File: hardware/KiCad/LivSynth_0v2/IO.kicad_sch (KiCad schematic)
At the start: 95 parts, among them J1 PJ398SM, J13 Jumper, J14 Jumper, J2 PJ398SM, J20 IDC, J3 PJ398SM, J4 IDC, Q6 2N3904, Q7 2N3904, SW6 SW_Push, U10 PCA9685PW, U11 PCA9685PW, U13 74HC165, U14 74HC165, U3 LM386

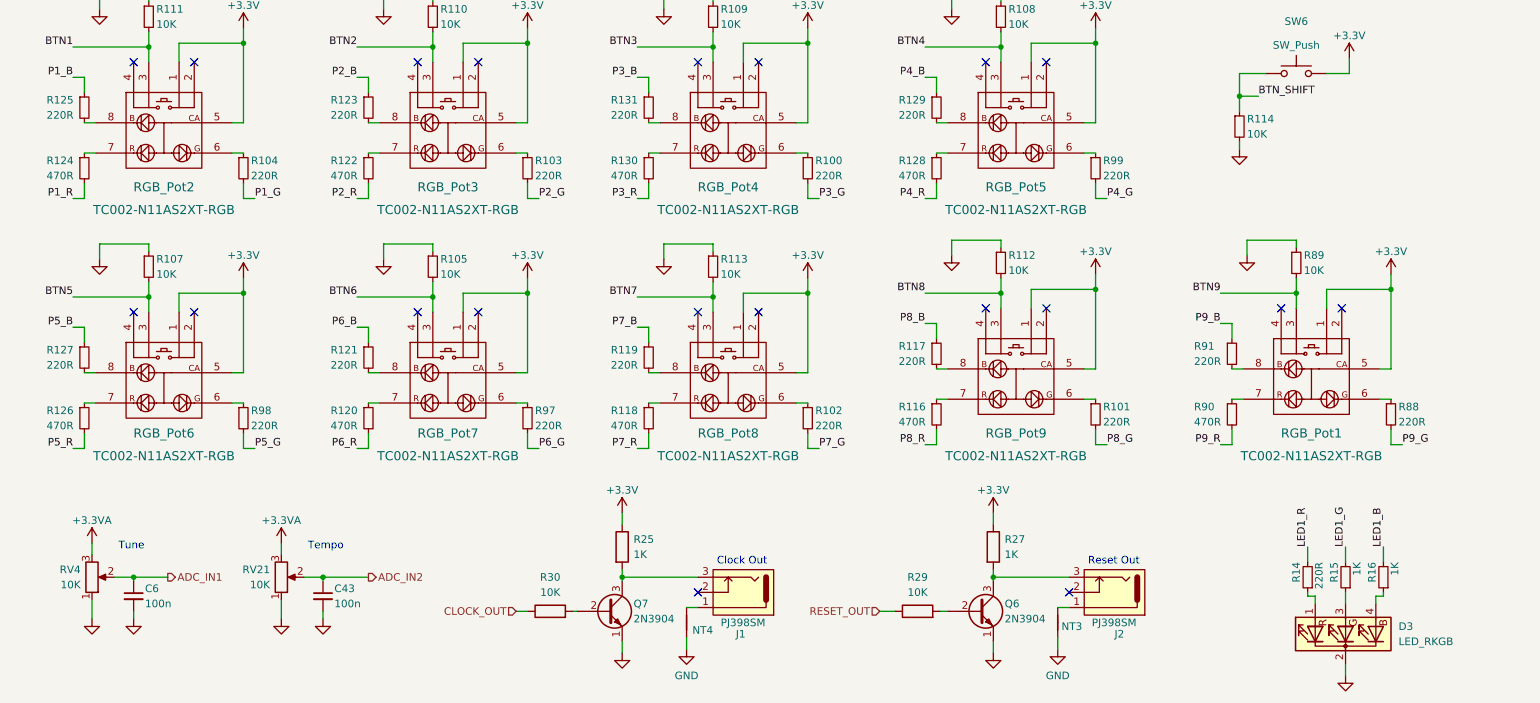
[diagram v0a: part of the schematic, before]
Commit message: Modify toggle switches (footprint and 3D model) Align R value designators Add JLC component placement checkup file
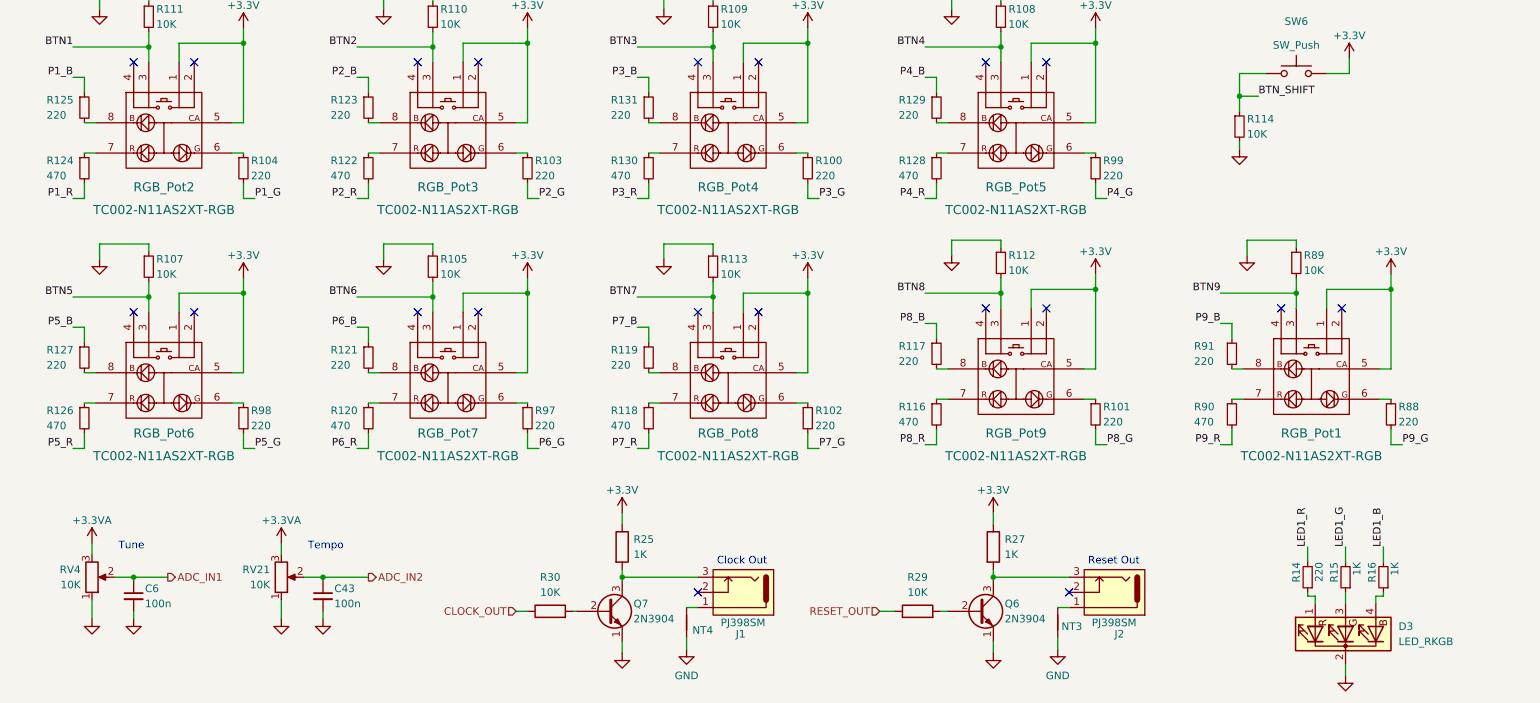
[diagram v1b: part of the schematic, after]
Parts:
- R100, R101, R102, R103, R104, R117, R119, R121, R123, R125, R127, R129, R131, R14, R88, R91, R97, R98, R99: value 220R -> 220
- R116, R118, R120, R122, R124, R126, R128, R130, R90: value 470R -> 470
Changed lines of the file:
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@@
       (effects (font (size 1.27 1.27)) (justify left))
     )
-    (property "Value" "220R" (id 1) (at 194.31 158.115 0)
+    (property "Value" "220" (id 1) (at 194.31 158.115 0)
       (effects (font (size 1.27 1.27)) (justify left))
     )
@@
       (effects (font (size 1.27 1.27)) (justify left))
     )
-    (property "Value" "220R" (id 1) (at 209.55 147.955 0)
+    (property "Value" "220" (id 1) (at 209.55 147.955 0)
       (effects (font (size 1.27 1.27)) (justify left))
     )
@@
       (effects (font (size 1.27 1.27)) (justify left))
     )
-    (property "Value" "220R" (id 1) (at 111.76 106.68 0)
+    (property "Value" "220" (id 1) (at 111.76 106.68 0)
       (effects (font (size 1.27 1.27)) (justify left))
     )
@@
       (effects (font (size 1.27 1.27)) (justify left))
     )
-    (property "Value" "220R" (id 1) (at 230.505 181.61 90)
+    (property "Value" "220" (id 1) (at 230.505 181.61 90)
       (effects (font (size 1.27 1.27)) (justify left))
     )
@@
       (effects (font (size 1.27 1.27)) (justify left))
     )
-    (property "Value" "220R" (id 1) (at 51.435 116.84 0)
+    (property "Value" "220" (id 1) (at 51.435 116.84 0)
       (effects (font (size 1.27 1.27)) (justify left))
     )
@@
       (effects (font (size 1.27 1.27)) (justify left))
     )
-    (property "Value" "470R" (id 1) (at 111.76 158.75 0)
+    (property "Value" "470" (id 1) (at 111.76 158.75 0)
       (effects (font (size 1.27 1.27)) (justify left))
     )
@@
       (effects (font (size 1.27 1.27)) (justify left))
     )
-    (property "Value" "220R" (id 1) (at 160.02 147.955 0)
+    (property "Value" "220" (id 1) (at 160.02 147.955 0)
       (effects (font (size 1.27 1.27)) (justify left))
     )
@@
       (effects (font (size 1.27 1.27)) (justify left))
     )
-    (property "Value" "220R" (id 1) (at 146.05 158.75 0)
+    (property "Value" "220" (id 1) (at 146.05 158.75 0)
       (effects (font (size 1.27 1.27)) (justify left))
     )
@@
       (effects (font (size 1.27 1.27)) (justify left))
     )
-    (property "Value" "220R" (id 1) (at 111.76 148.59 0)
+    (property "Value" "220" (id 1) (at 111.76 148.59 0)
       (effects (font (size 1.27 1.27)) (justify left))
     )
@@
       (effects (font (size 1.27 1.27)) (justify left))
     )
-    (property "Value" "220R" (id 1) (at 99.06 158.75 0)
+    (property "Value" "220" (id 1) (at 99.06 158.75 0)
       (effects (font (size 1.27 1.27)) (justify left))
     )
@@
       (effects (font (size 1.27 1.27)) (justify left))
     )
-    (property "Value" "470R" (id 1) (at 209.55 158.115 0)
+    (property "Value" "470" (id 1) (at 209.55 158.115 0)
       (effects (font (size 1.27 1.27)) (justify left))
     )
@@
       (effects (font (size 1.27 1.27)) (justify left))
     )
-    (property "Value" "220R" (id 1) (at 64.77 148.59 0)
+    (property "Value" "220" (id 1) (at 64.77 148.59 0)
       (effects (font (size 1.27 1.27)) (justify left))
     )
@@
       (effects (font (size 1.27 1.27)) (justify left))
     )
-    (property "Value" "220R" (id 1) (at 194.31 116.84 0)
+    (property "Value" "220" (id 1) (at 194.31 116.84 0)
       (effects (font (size 1.27 1.27)) (justify left))
     )
@@
       (effects (font (size 1.27 1.27)) (justify left))
     )
-    (property "Value" "220R" (id 1) (at 17.145 106.68 0)
+    (property "Value" "220" (id 1) (at 17.145 106.68 0)
       (effects (font (size 1.27 1.27)) (justify left))
     )
@@
       (effects (font (size 1.27 1.27)) (justify left))
     )
-    (property "Value" "220R" (id 1) (at 51.435 158.75 0)
+    (property "Value" "220" (id 1) (at 51.435 158.75 0)
       (effects (font (size 1.27 1.27)) (justify left))
     )
@@
       (effects (font (size 1.27 1.27)) (justify left))
     )
-    (property "Value" "470R" (id 1) (at 111.76 116.84 0)
+    (property "Value" "470" (id 1) (at 111.76 116.84 0)
       (effects (font (size 1.27 1.27)) (justify left))
     )
@@
       (effects (font (size 1.27 1.27)) (justify left))
     )
-    (property "Value" "470R" (id 1) (at 17.145 116.84 0)
+    (property "Value" "470" (id 1) (at 17.145 116.84 0)
       (effects (font (size 1.27 1.27)) (justify left))
     )
@@
       (effects (font (size 1.27 1.27)) (justify left))
     )
-    (property "Value" "220R" (id 1) (at 243.84 158.115 0)
+    (property "Value" "220" (id 1) (at 243.84 158.115 0)
       (effects (font (size 1.27 1.27)) (justify left))
     )
@@
       (effects (font (size 1.27 1.27)) (justify left))
     )
-    (property "Value" "220R" (id 1) (at 99.06 116.84 0)
+    (property "Value" "220" (id 1) (at 99.06 116.84 0)
       (effects (font (size 1.27 1.27)) (justify left))
     )
@@
       (effects (font (size 1.27 1.27)) (justify left))
     )
-    (property "Value" "470R" (id 1) (at 64.77 116.84 0)
+    (property "Value" "470" (id 1) (at 64.77 116.84 0)
       (effects (font (size 1.27 1.27)) (justify left))
     )
@@
       (effects (font (size 1.27 1.27)) (justify left))
     )
-    (property "Value" "470R" (id 1) (at 64.77 158.75 0)
+    (property "Value" "470" (id 1) (at 64.77 158.75 0)
       (effects (font (size 1.27 1.27)) (justify left))
     )
@@
       (effects (font (size 1.27 1.27)) (justify left))
     )
-    (property "Value" "220R" (id 1) (at 160.02 106.68 0)
+    (property "Value" "220" (id 1) (at 160.02 106.68 0)
       (effects (font (size 1.27 1.27)) (justify left))
     )
@@
       (effects (font (size 1.27 1.27)) (justify left))
     )
-    (property "Value" "220R" (id 1) (at 146.05 116.84 0)
+    (property "Value" "220" (id 1) (at 146.05 116.84 0)
       (effects (font (size 1.27 1.27)) (justify left))
     )
@@
       (effects (font (size 1.27 1.27)) (justify left))
     )
-    (property "Value" "470R" (id 1) (at 160.02 116.84 0)
+    (property "Value" "470" (id 1) (at 160.02 116.84 0)
       (effects (font (size 1.27 1.27)) (justify left))
     )
@@
       (effects (font (size 1.27 1.27)) (justify left))
     )
-    (property "Value" "220R" (id 1) (at 64.77 106.68 0)
+    (property "Value" "220" (id 1) (at 64.77 106.68 0)
       (effects (font (size 1.27 1.27)) (justify left))
     )
@@
       (effects (font (size 1.27 1.27)) (justify left))
     )
-    (property "Value" "470R" (id 1) (at 160.02 158.115 0)
+    (property "Value" "470" (id 1) (at 160.02 158.115 0)
       (effects (font (size 1.27 1.27)) (justify left))
     )
@@
       (effects (font (size 1.27 1.27)) (justify left))
     )
-    (property "Value" "220R" (id 1) (at 17.145 148.59 0)
+    (property "Value" "220" (id 1) (at 17.145 148.59 0)
       (effects (font (size 1.27 1.27)) (justify left))
     )
@@
       (effects (font (size 1.27 1.27)) (justify left))
     )
-    (property "Value" "470R" (id 1) (at 17.145 158.75 0)
-      (effects (font (size 1.27 1.27)) (justify left))
-    )
+    (property "Value" "470" (id 1) (at 17.145 158.75 0)
+      (effects (font (size 1.27 1.27)) (justify left))
+    )

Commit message: Create new 0v3 folder
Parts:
- R100, R101, R102, R103, R104, R117, R119, R121, R123, R125, R127, R129, R131, R14, R88, R91, R97, R98, R99: value 220 -> 220R
- R116, R118, R120, R122, R124, R126, R128, R130, R90: value 470 -> 470R
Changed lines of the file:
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@@
       (effects (font (size 1.27 1.27)) (justify left))
     )
-    (property "Value" "220" (id 1) (at 194.31 158.115 0)
+    (property "Value" "220R" (id 1) (at 194.31 158.115 0)
       (effects (font (size 1.27 1.27)) (justify left))
     )
@@
       (effects (font (size 1.27 1.27)) (justify left))
     )
-    (property "Value" "220" (id 1) (at 209.55 147.955 0)
+    (property "Value" "220R" (id 1) (at 209.55 147.955 0)
       (effects (font (size 1.27 1.27)) (justify left))
     )
@@
       (effects (font (size 1.27 1.27)) (justify left))
     )
-    (property "Value" "220" (id 1) (at 111.76 106.68 0)
+    (property "Value" "220R" (id 1) (at 111.76 106.68 0)
       (effects (font (size 1.27 1.27)) (justify left))
     )
@@
       (effects (font (size 1.27 1.27)) (justify left))
     )
-    (property "Value" "220" (id 1) (at 230.505 181.61 90)
+    (property "Value" "220R" (id 1) (at 230.505 181.61 90)
       (effects (font (size 1.27 1.27)) (justify left))
     )
@@
       (effects (font (size 1.27 1.27)) (justify left))
     )
-    (property "Value" "220" (id 1) (at 51.435 116.84 0)
+    (property "Value" "220R" (id 1) (at 51.435 116.84 0)
       (effects (font (size 1.27 1.27)) (justify left))
     )
@@
       (effects (font (size 1.27 1.27)) (justify left))
     )
-    (property "Value" "470" (id 1) (at 111.76 158.75 0)
+    (property "Value" "470R" (id 1) (at 111.76 158.75 0)
       (effects (font (size 1.27 1.27)) (justify left))
     )
@@
       (effects (font (size 1.27 1.27)) (justify left))
     )
-    (property "Value" "220" (id 1) (at 160.02 147.955 0)
+    (property "Value" "220R" (id 1) (at 160.02 147.955 0)
       (effects (font (size 1.27 1.27)) (justify left))
     )
@@
       (effects (font (size 1.27 1.27)) (justify left))
     )
-    (property "Value" "220" (id 1) (at 146.05 158.75 0)
+    (property "Value" "220R" (id 1) (at 146.05 158.75 0)
       (effects (font (size 1.27 1.27)) (justify left))
     )
@@
       (effects (font (size 1.27 1.27)) (justify left))
     )
-    (property "Value" "220" (id 1) (at 111.76 148.59 0)
+    (property "Value" "220R" (id 1) (at 111.76 148.59 0)
       (effects (font (size 1.27 1.27)) (justify left))
     )
@@
       (effects (font (size 1.27 1.27)) (justify left))
     )
-    (property "Value" "220" (id 1) (at 99.06 158.75 0)
+    (property "Value" "220R" (id 1) (at 99.06 158.75 0)
       (effects (font (size 1.27 1.27)) (justify left))
     )
@@
       (effects (font (size 1.27 1.27)) (justify left))
     )
-    (property "Value" "470" (id 1) (at 209.55 158.115 0)
+    (property "Value" "470R" (id 1) (at 209.55 158.115 0)
       (effects (font (size 1.27 1.27)) (justify left))
     )
@@
       (effects (font (size 1.27 1.27)) (justify left))
     )
-    (property "Value" "220" (id 1) (at 64.77 148.59 0)
+    (property "Value" "220R" (id 1) (at 64.77 148.59 0)
       (effects (font (size 1.27 1.27)) (justify left))
     )
@@
       (effects (font (size 1.27 1.27)) (justify left))
     )
-    (property "Value" "220" (id 1) (at 194.31 116.84 0)
+    (property "Value" "220R" (id 1) (at 194.31 116.84 0)
       (effects (font (size 1.27 1.27)) (justify left))
     )
@@
       (effects (font (size 1.27 1.27)) (justify left))
     )
-    (property "Value" "220" (id 1) (at 17.145 106.68 0)
+    (property "Value" "220R" (id 1) (at 17.145 106.68 0)
       (effects (font (size 1.27 1.27)) (justify left))
     )
@@
       (effects (font (size 1.27 1.27)) (justify left))
     )
-    (property "Value" "220" (id 1) (at 51.435 158.75 0)
+    (property "Value" "220R" (id 1) (at 51.435 158.75 0)
       (effects (font (size 1.27 1.27)) (justify left))
     )
@@
       (effects (font (size 1.27 1.27)) (justify left))
     )
-    (property "Value" "470" (id 1) (at 111.76 116.84 0)
+    (property "Value" "470R" (id 1) (at 111.76 116.84 0)
       (effects (font (size 1.27 1.27)) (justify left))
     )
@@
       (effects (font (size 1.27 1.27)) (justify left))
     )
-    (property "Value" "470" (id 1) (at 17.145 116.84 0)
+    (property "Value" "470R" (id 1) (at 17.145 116.84 0)
       (effects (font (size 1.27 1.27)) (justify left))
     )
@@
       (effects (font (size 1.27 1.27)) (justify left))
     )
-    (property "Value" "220" (id 1) (at 243.84 158.115 0)
+    (property "Value" "220R" (id 1) (at 243.84 158.115 0)
       (effects (font (size 1.27 1.27)) (justify left))
     )
@@
       (effects (font (size 1.27 1.27)) (justify left))
     )
-    (property "Value" "220" (id 1) (at 99.06 116.84 0)
+    (property "Value" "220R" (id 1) (at 99.06 116.84 0)
       (effects (font (size 1.27 1.27)) (justify left))
     )
@@
       (effects (font (size 1.27 1.27)) (justify left))
     )
-    (property "Value" "470" (id 1) (at 64.77 116.84 0)
+    (property "Value" "470R" (id 1) (at 64.77 116.84 0)
       (effects (font (size 1.27 1.27)) (justify left))
     )
@@
       (effects (font (size 1.27 1.27)) (justify left))
     )
-    (property "Value" "470" (id 1) (at 64.77 158.75 0)
+    (property "Value" "470R" (id 1) (at 64.77 158.75 0)
       (effects (font (size 1.27 1.27)) (justify left))
     )
@@
       (effects (font (size 1.27 1.27)) (justify left))
     )
-    (property "Value" "220" (id 1) (at 160.02 106.68 0)
+    (property "Value" "220R" (id 1) (at 160.02 106.68 0)
       (effects (font (size 1.27 1.27)) (justify left))
     )
@@
       (effects (font (size 1.27 1.27)) (justify left))
     )
-    (property "Value" "220" (id 1) (at 146.05 116.84 0)
+    (property "Value" "220R" (id 1) (at 146.05 116.84 0)
       (effects (font (size 1.27 1.27)) (justify left))
     )
@@
       (effects (font (size 1.27 1.27)) (justify left))
     )
-    (property "Value" "470" (id 1) (at 160.02 116.84 0)
+    (property "Value" "470R" (id 1) (at 160.02 116.84 0)
       (effects (font (size 1.27 1.27)) (justify left))
     )
@@
       (effects (font (size 1.27 1.27)) (justify left))
     )
-    (property "Value" "220" (id 1) (at 64.77 106.68 0)
+    (property "Value" "220R" (id 1) (at 64.77 106.68 0)
       (effects (font (size 1.27 1.27)) (justify left))
     )
@@
       (effects (font (size 1.27 1.27)) (justify left))
     )
-    (property "Value" "470" (id 1) (at 160.02 158.115 0)
+    (property "Value" "470R" (id 1) (at 160.02 158.115 0)
       (effects (font (size 1.27 1.27)) (justify left))
     )
@@
       (effects (font (size 1.27 1.27)) (justify left))
     )
-    (property "Value" "220" (id 1) (at 17.145 148.59 0)
+    (property "Value" "220R" (id 1) (at 17.145 148.59 0)
       (effects (font (size 1.27 1.27)) (justify left))
     )
@@
       (effects (font (size 1.27 1.27)) (justify left))
     )
-    (property "Value" "470" (id 1) (at 17.145 158.75 0)
-      (effects (font (size 1.27 1.27)) (justify left))
-    )
+    (property "Value" "470R" (id 1) (at 17.145 158.75 0)
+      (effects (font (size 1.27 1.27)) (justify left))
+    )
